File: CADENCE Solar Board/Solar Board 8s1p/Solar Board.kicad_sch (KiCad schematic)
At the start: 20 parts, among them J1 Conn_01x08, U1 INA230AIRGTT, U2 AD7414ARTZ-1REEL7, U3 OPT3001IDNPRQ1

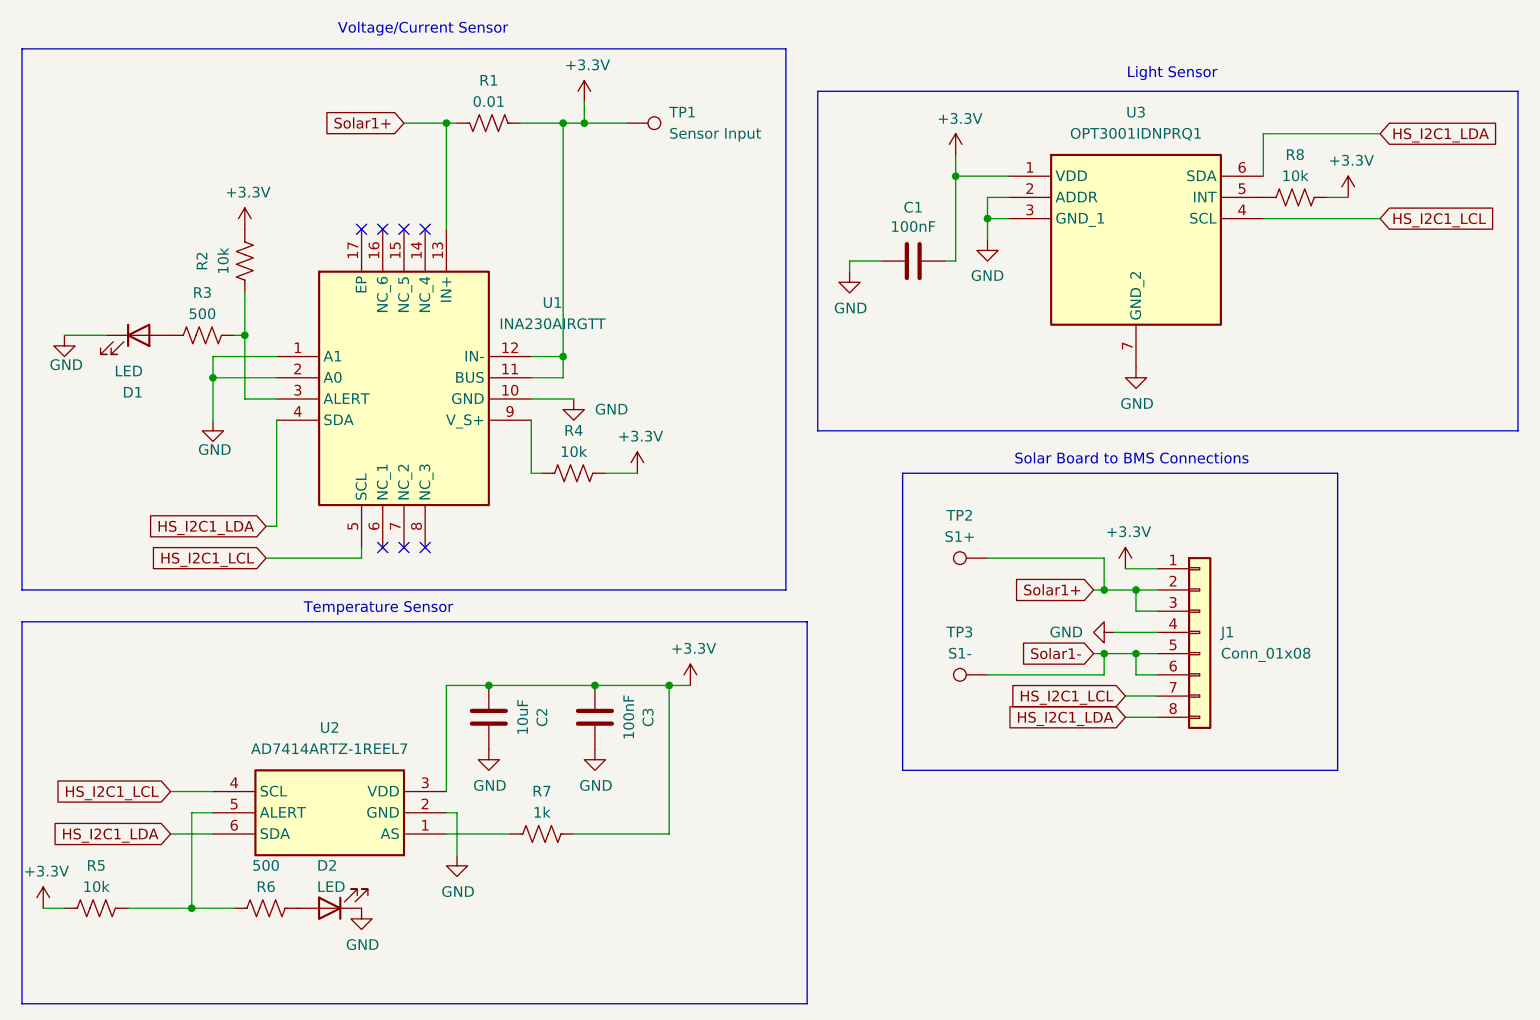
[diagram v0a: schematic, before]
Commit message: Updates
removed light sensor, changed pcb design, added screw holes for 8s1p and 8s2p configurations, optimized via paths in pcb
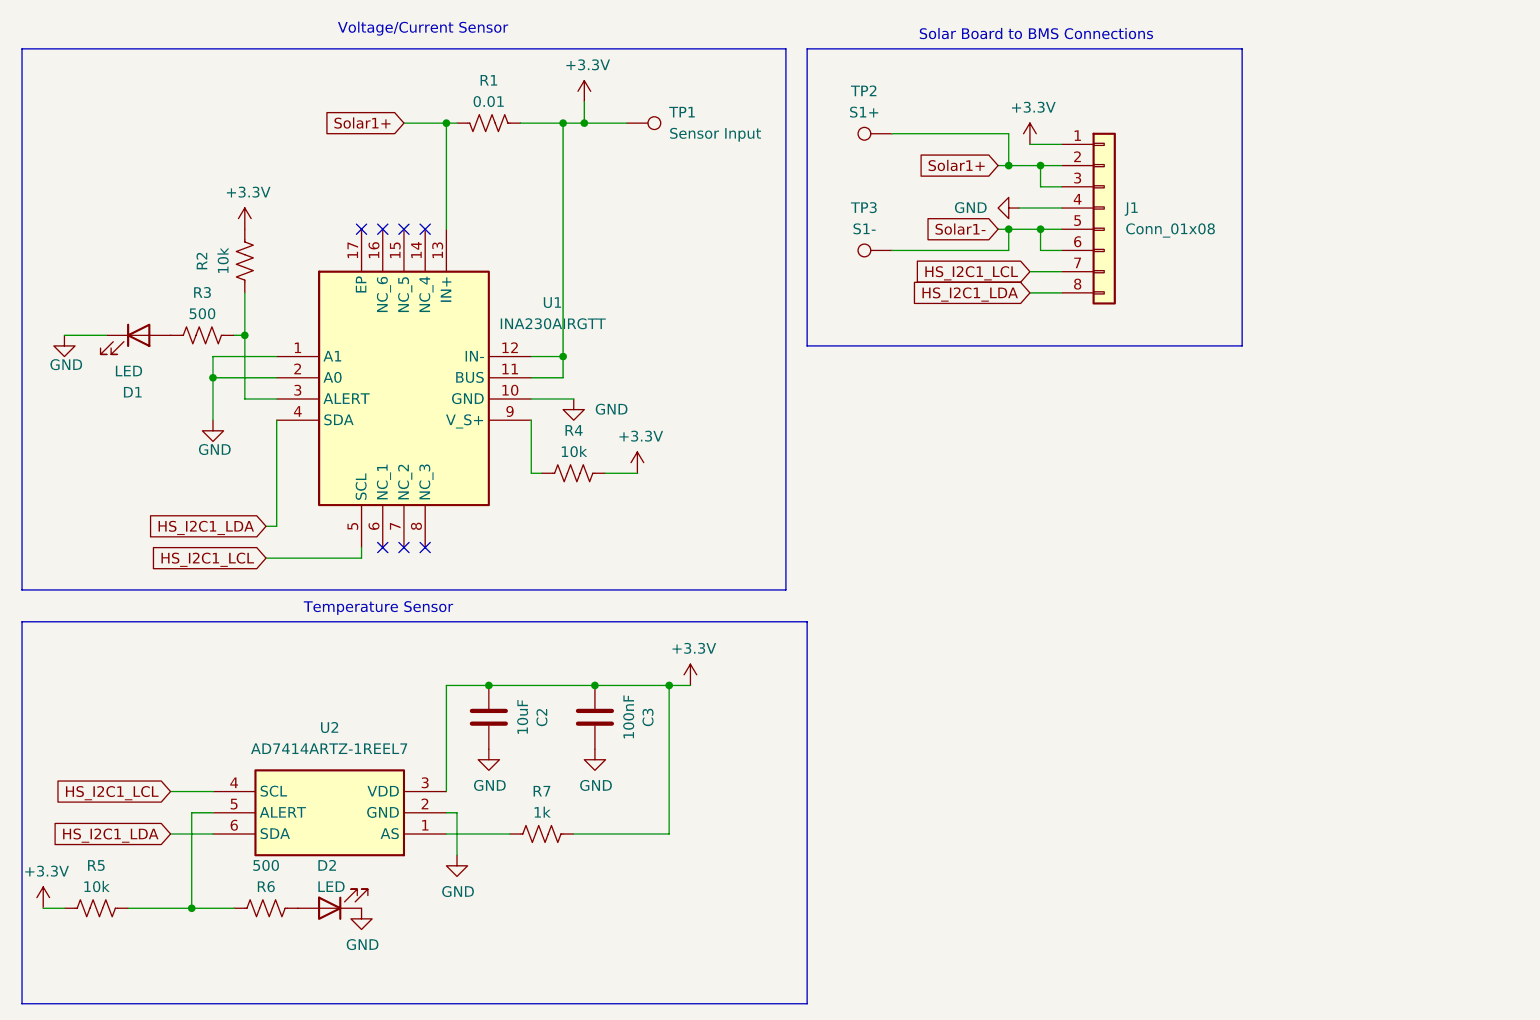
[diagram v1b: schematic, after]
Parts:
- removed C1: 100nF, Capacitor_SMD:C_0805_2012Metric, symbol Device:C
- removed R8: 10k, Resistor_SMD:R_0805_2012Metric, symbol Device:R_US
- removed U3: OPT3001IDNPRQ1, OPT3001IDNPRQ1:SON65P200X200X65-7N-D, symbol New_Library_0:OPT3001IDNPRQ1
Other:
- note removed: "Light Sensor"
- moved on the sheet: J1, TP2, TP3
